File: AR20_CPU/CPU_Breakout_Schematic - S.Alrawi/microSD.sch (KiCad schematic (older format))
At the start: 6 parts, among them U1 74LCX125M, U2 MCP1700_SOT23

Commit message: 4 Layers PCB is 90% finished
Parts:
- renumbered C17 to C12, C18 to C13
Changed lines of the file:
@@
 $Descr A4 11693 8268
 encoding utf-8
-Sheet 5 6
+Sheet 4 6
 Title ""
 Date ""
@@
 AR Path="/5DFCE3D9" Ref="U?"  Part="1"
 AR Path="/5DFCB53C/5DFCE3D9" Ref="U2"  Part="1"
+AR Path="/5DE8C4DF/5DFCE3D9" Ref="U2"  Part="1"
 F 0 "U2" H 8300 3649 50  0000 C CNN
 F 1 "MCP1700_SOT23" H 8300 3740 50  0000 C CNN
@@
 Wire Wire Line
 	6150 3400 6150 3500
-$Comp
-L Device:R R?
-U 1 1 5DFCE3E4
-P 6150 3650
-AR Path="/5DFCE3E4" Ref="R?"  Part="1"
-AR Path="/5DFCB53C/5DFCE3E4" Ref="R18"  Part="1"
-F 0 "R18" H 6220 3696 50  0000 L CNN
-F 1 "10k" H 6220 3605 50  0000 L CNN
-F 2 "Resistor_SMD:R_0603_1608Metric" V 6080 3650 50  0001 C CNN
-F 3 "~" H 6150 3650 50  0001 C CNN
-	1    6150 3650
-	1    0    0    -1
-$EndComp
 Wire Wire Line
 	5950 1800 5950 1700
@@
 AR Path="/5DFCE3F6" Ref="SDcard?"  Part="1"
 AR Path="/5DFCB53C/5DFCE3F6" Ref="SDcard1"  Part="1"
+AR Path="/5DE8C4DF/5DFCE3F6" Ref="SDcard1"  Part="1"
 F 0 "SDcard1" H 5300 3317 50  0000 C CNN
 F 1 "Micro_SD_Card" H 5300 3226 50  0000 C CNN
@@
 	3750 3750 3800 3750
 $Comp
-L Device:C C18
+L Device:C C13
 U 1 1 5DE59DD0
 P 8900 3650
-F 0 "C18" H 8785 3604 50  0000 R CNN
+F 0 "C13" H 8785 3604 50  0000 R CNN
 F 1 "100u" H 8785 3695 50  0000 R CNN
 F 2 "Capacitor_SMD:C_0603_1608Metric" H 8938 3500 50  0001 C CNN
@@
 $EndComp
 $Comp
-L Device:C C17
+L Device:C C12
 U 1 1 5DE5A450
 P 7750 3650
-F 0 "C17" H 7635 3604 50  0000 R CNN
+F 0 "C12" H 7635 3604 50  0000 R CNN
 F 1 "100u" H 7635 3695 50  0000 R CNN
 F 2 "Capacitor_SMD:C_0603_1608Metric" H 7788 3500 50  0001 C CNN
@@
 Wire Wire Line
 	8300 3800 8900 3800
+$Comp
+L Device:R R?
+U 1 1 5DFCE3E4
+P 6150 3650
+AR Path="/5DFCE3E4" Ref="R?"  Part="1"
+AR Path="/5DFCB53C/5DFCE3E4" Ref="R18"  Part="1"
+AR Path="/5DE8C4DF/5DFCE3E4" Ref="R19"  Part="1"
+F 0 "R19" H 6220 3696 50  0000 L CNN
+F 1 "10k" H 6220 3605 50  0000 L CNN
+F 2 "Resistor_SMD:R_0603_1608Metric" V 6080 3650 50  0001 C CNN
+F 3 "~" H 6150 3650 50  0001 C CNN
+	1    6150 3650
+	1    0    0    -1
+$EndComp
 $EndSCHEMATC

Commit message: BreakoutBoard final edit
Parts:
- removed R18: 10k, Resistor_SMD:R_0603_1608Metric, symbol Device:R
- removed U1: 74LCX125M, SOIC127P600X175-14N, symbol SamacSys_Parts:74LCX125M
- C12: value 100u -> 0.1u
- C13: value 100u -> 1u
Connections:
- net CS_3.3V is gone; now on net 10_CS: SDcard1.2 (DAT3/CD)
- net MOSI_3.3V is gone; now on net 11_MOSI: SDcard1.3 (CMD)
- net SCLK_3.3V is gone; now on net 13(LED): SDcard1.5 (CLK)
- net 3V3_SD renamed 3V3_OUT
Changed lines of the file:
@@
 	1    0    0    -1
 $EndComp
-Text GLabel 9100 3500 2    50   Input ~ 0
-3V3_SD
-Wire Wire Line
-	6150 3400 6150 3500
 Wire Wire Line
 	5950 1800 5950 1700
-Text GLabel 5350 3700 3    50   Input ~ 0
-3V3_SD
 Wire Wire Line
 	5250 3700 5250 3500
@@
 Wire Wire Line
 	5350 3700 5350 3500
-Wire Wire Line
-	5150 3700 5150 3500
-Text GLabel 3800 4250 2    50   Input ~ 0
-13(LED)
-Text GLabel 2500 3850 0    50   Input ~ 0
-10_CS
-Text GLabel 2500 4150 0    50   Input ~ 0
-11_MOSI
 Text GLabel 5650 3900 3    50   Input ~ 0
 12_MISO
+Text GLabel 5550 3700 3    50   Input ~ 0
+Ground
+Text GLabel 5950 1700 2    50   Input ~ 0
+Ground
+Wire Wire Line
+	7750 3800 8300 3800
+Connection ~ 8300 3800
+Wire Wire Line
+	8300 3800 8900 3800
+Wire Wire Line
+	7550 3500 7750 3500
+Wire Wire Line
+	8000 3500 7750 3500
+Connection ~ 7750 3500
+$Comp
+L Device:C C12
+U 1 1 5DE5A450
+P 7750 3650
+F 0 "C12" H 7635 3604 50  0000 R CNN
+F 1 "0.1u" H 7635 3695 50  0000 R CNN
+F 2 "Capacitor_SMD:C_0603_1608Metric" H 7788 3500 50  0001 C CNN
+F 3 "~" H 7750 3650 50  0001 C CNN
+	1    7750 3650
+	-1   0    0    1
+$EndComp
+Text GLabel 9100 3500 2    50   Input ~ 0
+3V3_OUT
+Wire Wire Line
+	8900 3500 8600 3500
+Wire Wire Line
+	9100 3500 8900 3500
+Connection ~ 8900 3500
+$Comp
+L Device:C C13
+U 1 1 5DE59DD0
+P 8900 3650
+F 0 "C13" H 8785 3604 50  0000 R CNN
+F 1 "1u" H 8785 3695 50  0000 R CNN
+F 2 "Capacitor_SMD:C_0603_1608Metric" H 8938 3500 50  0001 C CNN
+F 3 "~" H 8900 3650 50  0001 C CNN
+	1    8900 3650
+	-1   0    0    1
+$EndComp
+Text GLabel 5150 3700 3    50   Input ~ 0
+10_CS
+Text GLabel 5450 3700 3    50   Input ~ 0
+13(LED)
+Text GLabel 5250 3700 3    50   Input ~ 0
+11_MOSI
+Text GLabel 5350 3700 3    50   Input ~ 0
+3V3_OUT
+Wire Wire Line
+	5650 3500 5650 3900
 $Comp
 L Connector:Micro_SD_Card SDcard?
@@
 	0    -1   -1   0
 $EndComp
-Text GLabel 5550 3700 3    50   Input ~ 0
-Ground
-Text GLabel 5950 1700 2    50   Input ~ 0
-Ground
-Text GLabel 5150 3700 3    50   Input ~ 0
-CS_3.3V
-Text GLabel 2500 3950 0    50   Input ~ 0
-CS_3.3V
-Text GLabel 5250 3700 3    50   Input ~ 0
-MOSI_3.3V
-Text GLabel 2500 4250 0    50   Input ~ 0
-MOSI_3.3V
-Text GLabel 2500 4350 0    50   Input ~ 0
-Ground
-Text GLabel 5450 3700 3    50   Input ~ 0
-SCLK_3.3V
-Text GLabel 3800 4350 2    50   Input ~ 0
-SCLK_3.3V
-Text GLabel 3800 3750 2    50   Input ~ 0
-3V3_SD
-Text GLabel 2500 3750 0    50   Input ~ 0
-Ground
-Text GLabel 3800 4150 2    50   Input ~ 0
-Ground
 Wire Wire Line
-	3800 4350 3700 4350
-Wire Wire Line
-	3800 4250 3700 4250
-Wire Wire Line
-	3800 4150 3700 4150
-Wire Wire Line
-	2500 3750 2600 3750
-Wire Wire Line
-	2500 3850 2600 3850
-Wire Wire Line
-	2500 3950 2600 3950
-Wire Wire Line
-	2500 4150 2600 4150
-Wire Wire Line
-	2500 4250 2600 4250
-Wire Wire Line
-	2500 4350 2600 4350
-Text GLabel 2500 4050 0    50   Input ~ 0
-Ground
-Wire Wire Line
-	2600 4050 2500 4050
-Text GLabel 6150 3400 2    50   Input ~ 0
-3V3_SD
-Wire Wire Line
-	5650 3500 5650 3800
-Wire Wire Line
-	5650 3800 6150 3800
-Connection ~ 5650 3800
-Wire Wire Line
-	5650 3800 5650 3900
-$Comp
-L SamacSys_Parts:74LCX125M U1
-U 1 1 5DE57AC5
-P 2600 3750
-F 0 "U1" H 3150 4015 50  0000 C CNN
-F 1 "74LCX125M" H 3150 3924 50  0000 C CNN
-F 2 "SOIC127P600X175-14N" H 3550 3850 50  0001 L CNN
-F 3 "https://componentsearchengine.com/Datasheets/1/74LCX125M.pdf" H 3550 3750 50  0001 L CNN
-F 4 "Low Voltage Quad Buffer with 5V Tolerant Inputs and Outputs" H 3550 3650 50  0001 L CNN "Description"
-F 5 "" H 3550 3550 50  0001 L CNN "Height"
-F 6 "512-74LCX125M" H 3550 3450 50  0001 L CNN "Mouser Part Number"
-F 7 "https://www.mouser.com/Search/Refine.aspx?Keyword=512-74LCX125M" H 3550 3350 50  0001 L CNN "Mouser Price/Stock"
-F 8 "ON Semiconductor" H 3550 3250 50  0001 L CNN "Manufacturer_Name"
-F 9 "74LCX125M" H 3550 3150 50  0001 L CNN "Manufacturer_Part_Number"
-	1    2600 3750
-	1    0    0    -1
-$EndComp
-Wire Wire Line
-	3700 3850 3700 3950
-Wire Wire Line
-	3700 4050 3700 3950
-Connection ~ 3700 3950
-Wire Wire Line
-	3700 3750 3750 3750
-Wire Wire Line
-	3750 3750 3750 3950
-Wire Wire Line
-	3750 3950 3700 3950
-Connection ~ 3750 3750
-Wire Wire Line
-	3750 3750 3800 3750
-$Comp
-L Device:C C13
-U 1 1 5DE59DD0
-P 8900 3650
-F 0 "C13" H 8785 3604 50  0000 R CNN
-F 1 "100u" H 8785 3695 50  0000 R CNN
-F 2 "Capacitor_SMD:C_0603_1608Metric" H 8938 3500 50  0001 C CNN
-F 3 "~" H 8900 3650 50  0001 C CNN
-	1    8900 3650
-	-1   0    0    1
-$EndComp
-$Comp
-L Device:C C12
-U 1 1 5DE5A450
-P 7750 3650
-F 0 "C12" H 7635 3604 50  0000 R CNN
-F 1 "100u" H 7635 3695 50  0000 R CNN
-F 2 "Capacitor_SMD:C_0603_1608Metric" H 7788 3500 50  0001 C CNN
-F 3 "~" H 7750 3650 50  0001 C CNN
-	1    7750 3650
-	-1   0    0    1
-$EndComp
-Wire Wire Line
-	9100 3500 8900 3500
-Wire Wire Line
-	8900 3500 8600 3500
-Connection ~ 8900 3500
-Wire Wire Line
-	8000 3500 7750 3500
-Wire Wire Line
-	7550 3500 7750 3500
-Connection ~ 7750 3500
-Wire Wire Line
-	7750 3800 8300 3800
-Connection ~ 8300 3800
-Wire Wire Line
-	8300 3800 8900 3800
-$Comp
-L Device:R R?
-U 1 1 5DFCE3E4
-P 6150 3650
-AR Path="/5DFCE3E4" Ref="R?"  Part="1"
-AR Path="/5DFCB53C/5DFCE3E4" Ref="R18"  Part="1"
-AR Path="/5DE8C4DF/5DFCE3E4" Ref="R19"  Part="1"
-F 0 "R19" H 6220 3696 50  0000 L CNN
-F 1 "10k" H 6220 3605 50  0000 L CNN
-F 2 "Resistor_SMD:R_0603_1608Metric" V 6080 3650 50  0001 C CNN
-F 3 "~" H 6150 3650 50  0001 C CNN
-	1    6150 3650
-	1    0    0    -1
-$EndComp
+	5150 3500 5150 3700
 $EndSCHEMATC

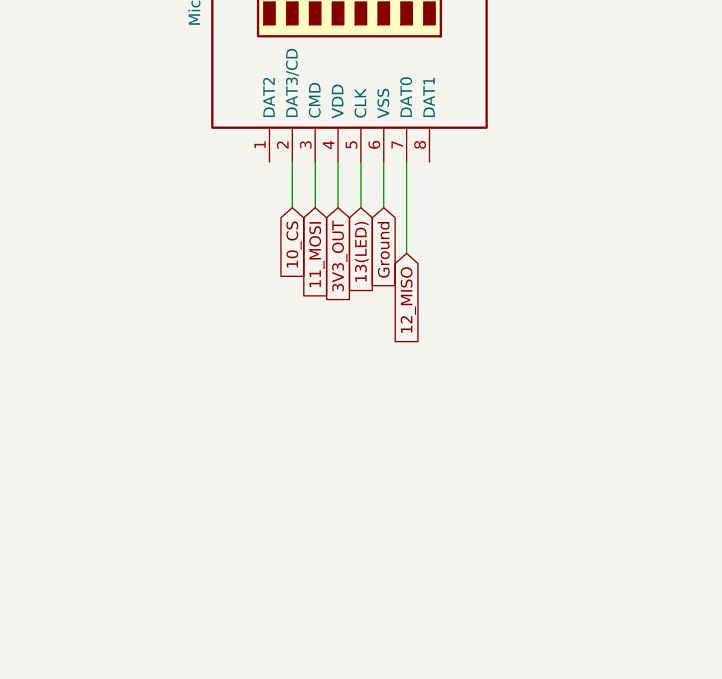
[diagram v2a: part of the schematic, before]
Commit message: Edited the Vreg  to SD
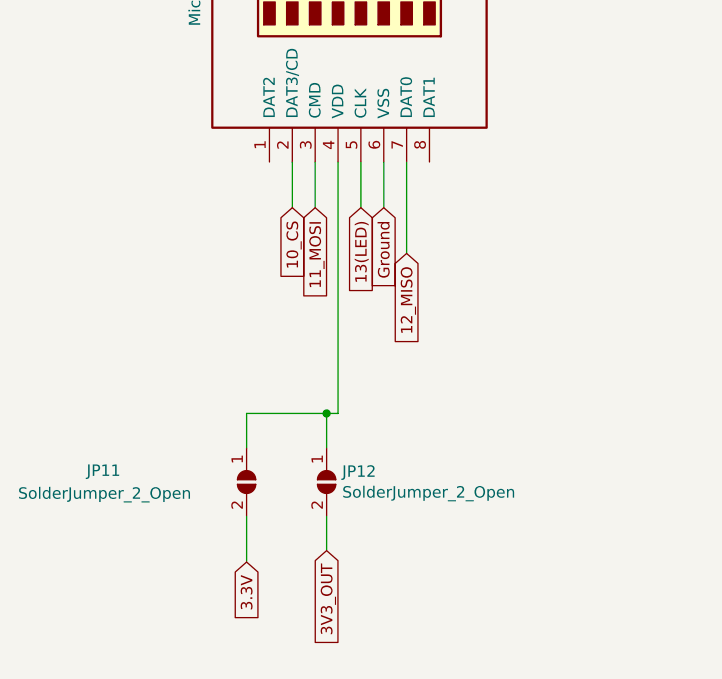
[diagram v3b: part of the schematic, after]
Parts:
- added JP11, JP12: SolderJumper_2_Open, Jumper:SolderJumper-2_P1.3mm_Open_RoundedPad1.0x1.5mm, symbol Jumper:SolderJumper_2_Open
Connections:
- net 3V3_OUT: now also JP12.2 (B); no longer SDcard1.4 (VDD)
- new net: JP11.1 (A), JP12.1 (A), SDcard1.4 (VDD)
- new net 3.3V: JP11.2 (B)
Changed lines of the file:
@@
 Wire Wire Line
 	5450 3700 5450 3500
-Wire Wire Line
-	5350 3700 5350 3500
 Text GLabel 5650 3900 3    50   Input ~ 0
 12_MISO
@@
 Text GLabel 5250 3700 3    50   Input ~ 0
 11_MOSI
-Text GLabel 5350 3700 3    50   Input ~ 0
+Text GLabel 5300 5200 3    50   Input ~ 0
 3V3_OUT
 Wire Wire Line
@@
 Wire Wire Line
 	5150 3500 5150 3700
+$Comp
+L Jumper:SolderJumper_2_Open JP12
+U 1 1 5DEFC778
+P 5300 4900
+F 0 "JP12" V 5254 4968 50  0000 L CNN
+F 1 "SolderJumper_2_Open" V 5345 4968 50  0000 L CNN
+F 2 "Jumper:SolderJumper-2_P1.3mm_Open_RoundedPad1.0x1.5mm" H 5300 4900 50  0001 C CNN
+F 3 "~" H 5300 4900 50  0001 C CNN
+	1    5300 4900
+	0    1    1    0
+$EndComp
+$Comp
+L Jumper:SolderJumper_2_Open JP11
+U 1 1 5DF02FDA
+P 4950 4900
+F 0 "JP11" V 4900 4200 50  0000 L CNN
+F 1 "SolderJumper_2_Open" V 5000 3900 50  0000 L CNN
+F 2 "Jumper:SolderJumper-2_P1.3mm_Open_RoundedPad1.0x1.5mm" H 4950 4900 50  0001 C CNN
+F 3 "~" H 4950 4900 50  0001 C CNN
+	1    4950 4900
+	0    1    1    0
+$EndComp
+Wire Wire Line
+	5300 5200 5300 5050
+Wire Wire Line
+	5300 4750 5300 4600
+Wire Wire Line
+	4950 4750 4950 4600
+Wire Wire Line
+	5350 4600 5300 4600
+Wire Wire Line
+	5350 3500 5350 4600
+Wire Wire Line
+	5300 4600 4950 4600
+Connection ~ 5300 4600
+Text GLabel 4950 5250 3    50   Input ~ 0
+3.3V
+Wire Wire Line
+	4950 5050 4950 5250
 $EndSCHEMATC
